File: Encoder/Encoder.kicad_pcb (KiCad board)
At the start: 2 copper layers, 50 x 40 mm, 58 parts, among them J1 Conn_01x02_Male, J2 Conn_01x04_Male, J3 Conn_01x04_Male, J4 Conn_01x04_Female, Q1 SSM3J332R, Q12 S8050, Q2 BSS138, Q3 SSM3J332R, SW1 SW_DIP_x05, SW2 SW_SPDT_White, SW3 SW_SPST, U1 AZ1084CD-3.3, U2 MAX3485, U3 AS5600, U4 STM32C011F4P6, Y1 48MHz

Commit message: 回路図pdf出力
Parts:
- C1: value 4.7uF -> 1uF; footprint Capacitor_SMD:C_0603_1608Metric -> Capacitor_SMD:C_0402_1005Metric
- D2, D3: footprint Diode_SMD:D_SMA_Handsoldering -> Diode_SMD:D_SMA
- JP1: footprint Connector_PinHeader_2.54mm:PinHeader_1x02_P2.54mm_Vertical -> Jumper:SolderJumper-2_P1.3mm_Open_TrianglePad1.0x1.5mm
- Q1, Q3, U1, U2, U4: moved to B.Cu
- Y1: footprint Crystal:Crystal_SMD_HC49-SD_HandSoldering -> Crystal:Crystal_SMD_HC49-SD; moved to B.Cu
- moved U2 86.3 mm to (-8.25, -45.8), turned to 180 degrees
- moved D5 84.7 mm to (-4.25, -56.5)
- moved D8 80.6 mm to (0.00, -56.5)
- moved D1 65.9 mm to (4.25, -56.5)
- moved U4 65.6 mm to (0.00, -38.2), turned to 90 degrees
- moved SW2 60.7 mm to (9.50, -41.8)
- moved SW3 55.9 mm to (-9.75, -42.0), turned to 90 degrees
- moved Y1 53.2 mm to (-8.50, -34.5), turned to -90 degrees
- moved U1 46.2 mm to (14.5, -69.8)
- moved Q3 41.3 mm to (32.0, -56.0), turned to 180 degrees
- moved Q1 39.7 mm to (36.2, -56.0), turned to 90 degrees
- moved J2 13.8 mm to (-10.2, -52.4)
- moved J1 12.8 mm to (7.50, -52.4)
- moved SW1 1.94 mm to (0.00, -43.0)
- moved U3 0.10 mm to (0.00, -30.0)

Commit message: 定期更新
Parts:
- C1, C12, C15, C2, C3, C4, C5, C6, C7, D2, D3, JP1, Q12, Q2, R1, R10, R12, R14, R2, R24, R27, R28, R29, R3, R30, R31, R32, R4, R5, R6, R7, R8, R9: moved to B.Cu
- moved R31 101.5 mm to (-8.91, -48.5)
- moved C5 99.5 mm to (-11.5, -28.5), turned to -90 degrees
- moved R29 98.8 mm to (-6.90, -41.1)
- moved C2 95.5 mm to (-4.38, -28.7), turned to 90 degrees
- moved C15 89.1 mm to (-8.92, -47.4)
- moved R24 88.0 mm to (0.00, -56.6), turned to 180 degrees
- moved C6 79.2 mm to (-11.5, -35.5), turned to 90 degrees
- moved JP1 75.8 mm to (-11.8, -48.6)
- moved Q2 75.1 mm to (9.65, -47.6)
- moved R2 74.2 mm to (18.6, -46.4), turned to 90 degrees
- moved C4 74.2 mm to (10.1, -33.7), turned to 180 degrees
- moved C12 72.8 mm to (-4.73, -37.3), turned to 180 degrees
- moved R28 72.7 mm to (-6.89, -46.1), turned to 180 degrees
- moved R10 69.3 mm to (11.1, -41.7), turned to -90 degrees
- moved C7 69.1 mm to (-4.63, -38.7), turned to 180 degrees
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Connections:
- U4 pad 2: unconnected-(U4-Pad2) -> OSC_IN
- U4 pad 3: unconnected-(U4-Pad3) -> OSC_OUT
- U4 pad 6: unconnected-(U4-Pad6) -> NRST
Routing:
- net OSC_IN: track 0.00 -> 0.69 mm

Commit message: 進捗
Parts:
- added H1: MountingHole_Pad, TestPoint:TestPoint_Pad_1.5x1.5mm, F.Cu at (49.1, -46.6)
- added H2: MountingHole_Pad, TestPoint:TestPoint_Pad_1.5x1.5mm, F.Cu at (45.5, -46.6)
- C8, C9: footprint Capacitor_SMD:C_0805_2012Metric_Pad1.18x1.45mm_HandSolder -> Capacitor_SMD:C_0805_2012Metric; moved to B.Cu
- D2, D3: value SBR1A40SA -> 1N5819WS; footprint Diode_SMD:D_SMA -> Diode_SMD:D_SOD-323_HandSoldering
- R11, R13: moved to B.Cu
- moved R11 56.8 mm to (19.6, -31.1), turned to -90 degrees
- moved C9 46.2 mm to (5.29, -24.3), turned to -90 degrees
- moved R1 36.4 mm to (-2.90, -48.1)
- moved R3 36.4 mm to (-2.90, -47.0)
- moved R6 36.4 mm to (-2.90, -44.7)
- moved R8 36.4 mm to (-2.90, -43.6)
- moved R5 36.4 mm to (-2.90, -45.8)
- moved R13 27.6 mm to (11.2, -35.6), turned to -90 degrees
- moved C8 25.0 mm to (17.7, -31.3), turned to -90 degrees
- moved Q2 11.5 mm to (21.1, -47.6), turned to -90 degrees
- moved R10 10.5 mm to (18.6, -49.1), turned to 90 degrees
- moved C4 8.96 mm to (7.08, -25.3), turned to -90 degrees
- moved C5 6.52 mm to (-12.3, -22.0), turned to 180 degrees
- moved Y1 5.69 mm to (-13.1, -29.8)
- moved C6 3.43 mm to (-14.0, -37.9), turned to 0 degrees
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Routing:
- net RS485_A: track 0.00 -> 25.5 mm
- net RS485_B: track 0.00 -> 19.8 mm
- net 主電源スイッチ: track 0.00 -> 9.49 mm
- net MainTX_RS485RX: track 0.00 -> 8.43 mm
- net Net-(Q12-Pad3): track 0.00 -> 8.43 mm
- net Net-(JP1-Pad2): track 0.00 -> 2.15 mm
- net Net-(Q12-Pad1): track 0.00 -> 1.77 mm
- net unconnected-(U4-Pad1): track 0.00 -> 0.69 mm
- net OSC_IN: track 0.69 -> 0.00 mm
- added copper zone on B.Cu, net /5VBAT
- added copper zone on B.Cu, net /S-S

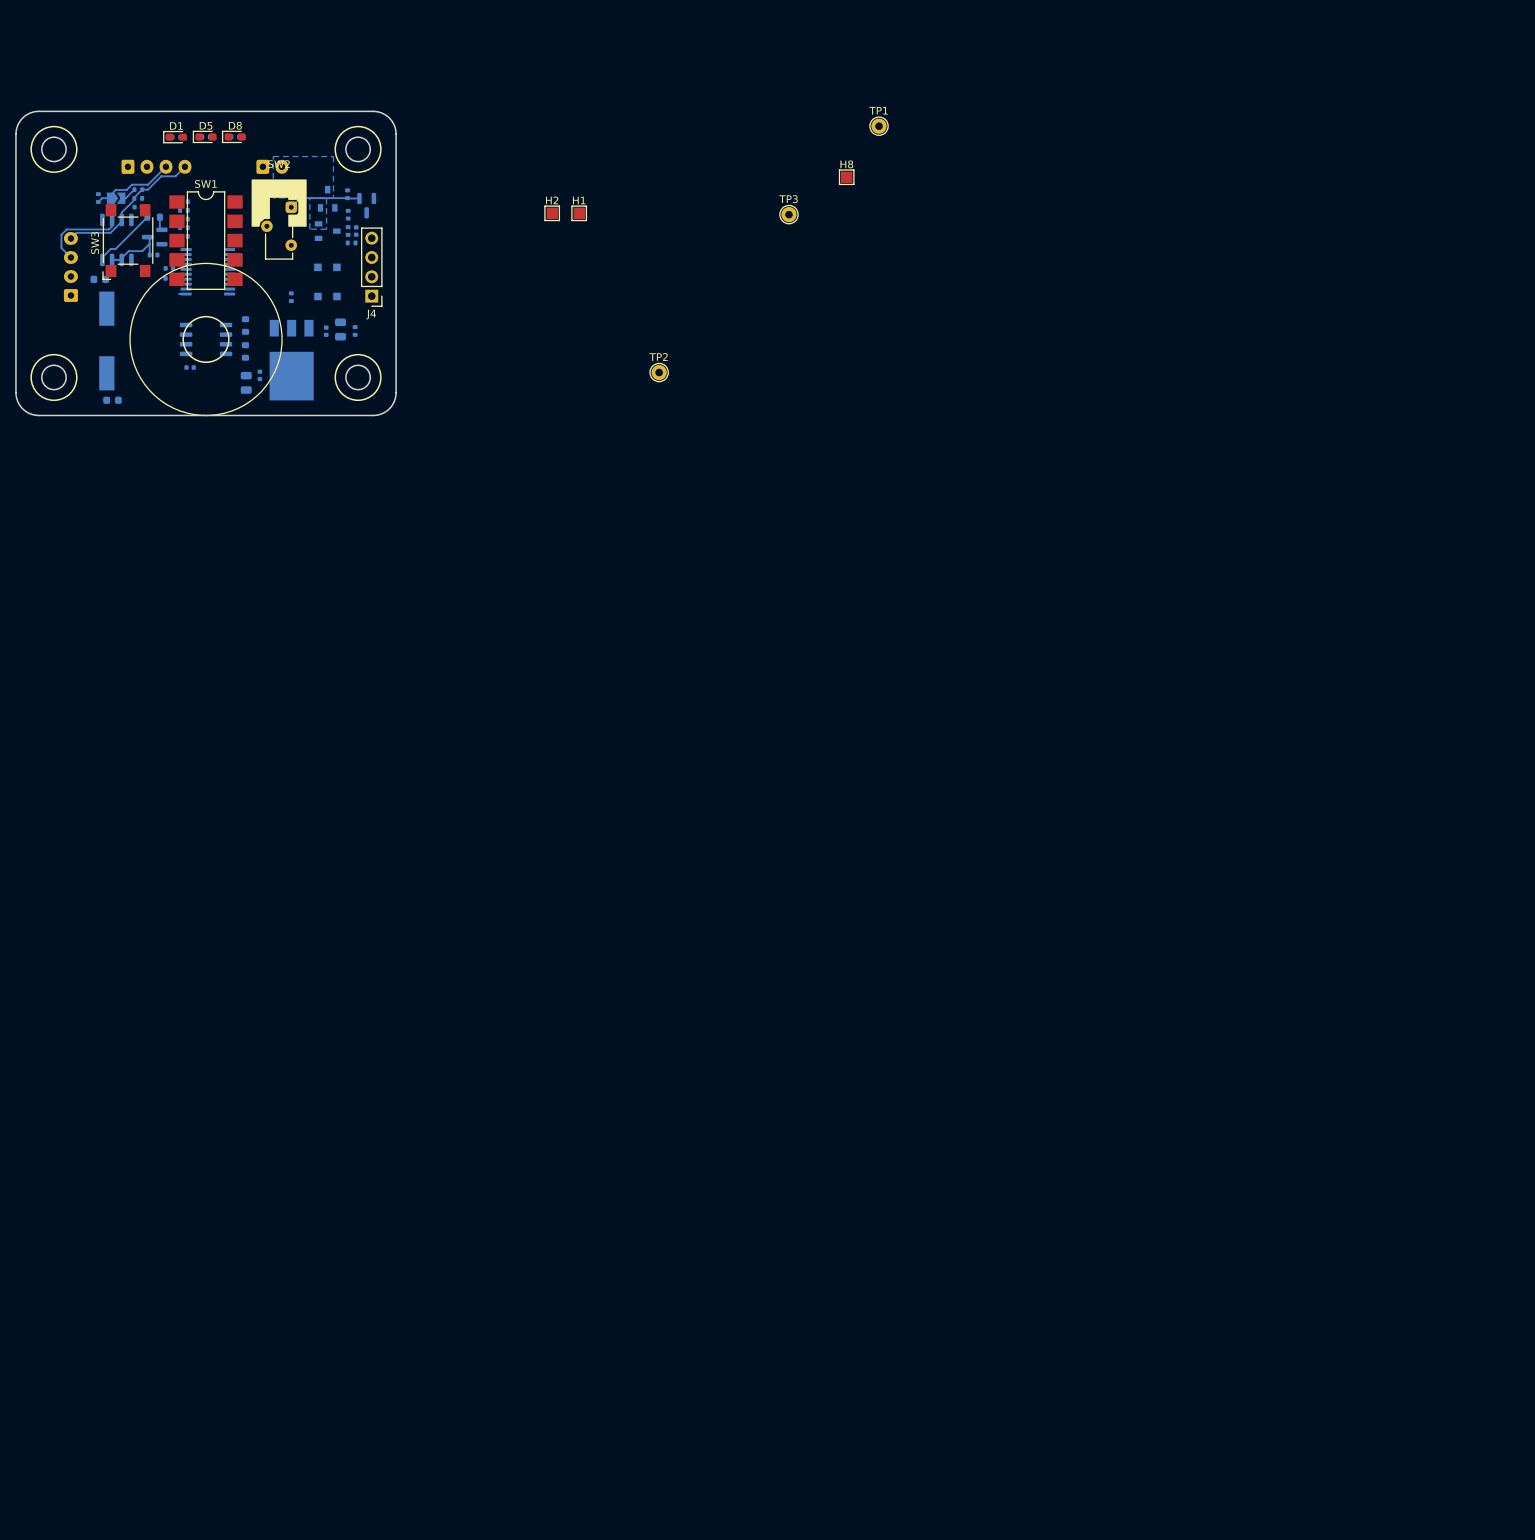
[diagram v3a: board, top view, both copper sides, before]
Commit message: エンコーダー基板配線完了
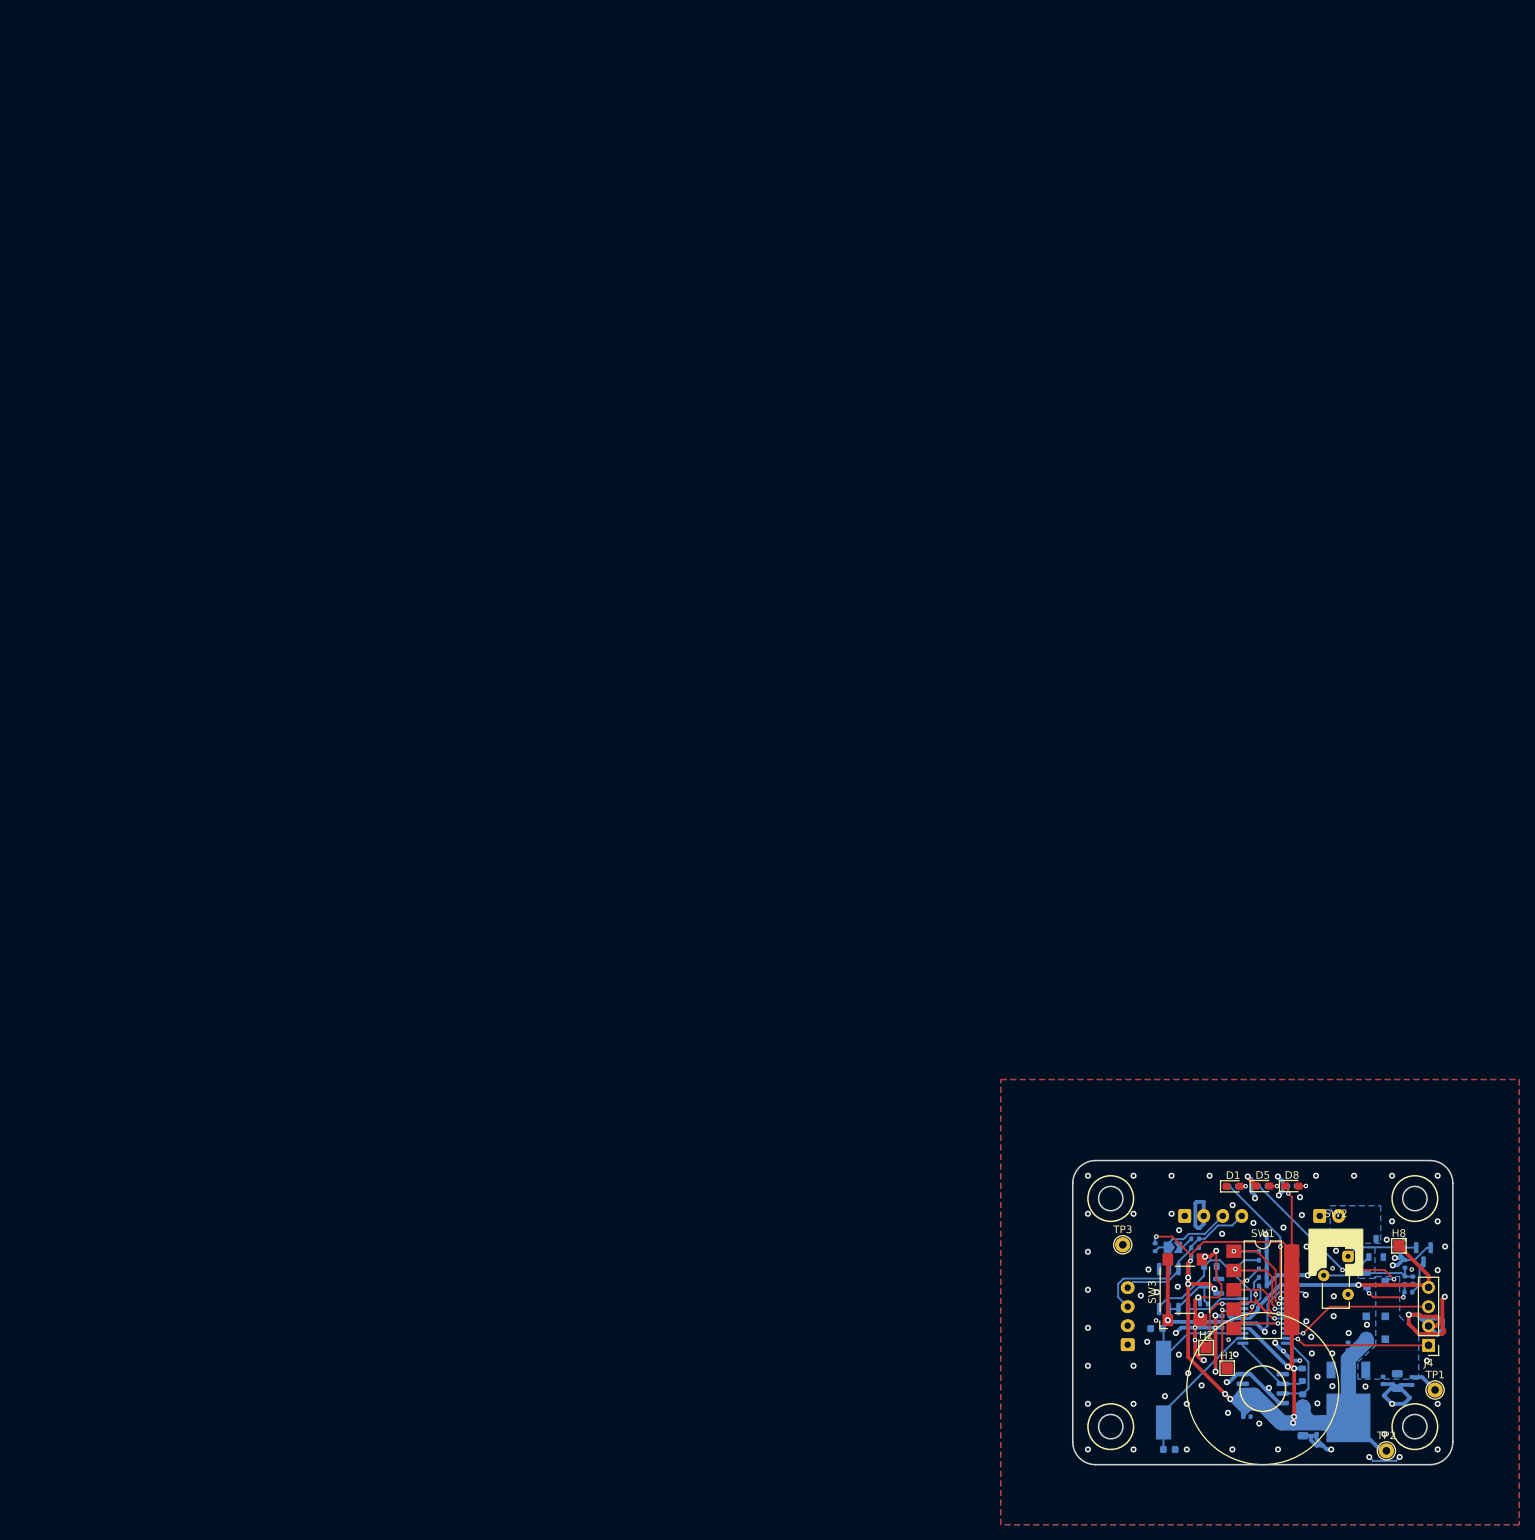
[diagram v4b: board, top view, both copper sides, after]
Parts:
- H1: value MountingHole_Pad -> UART1_TX
- H2: value MountingHole_Pad -> UART1_RX
- U4: value STM32C011F4P6 -> STM32C011F6P6
- moved R1 198.0 mm to (139.0, 90.0)
- moved R3 198.0 mm to (139.0, 91.1)
- moved R5 198.0 mm to (139.0, 92.2)
- moved R6 198.0 mm to (139.0, 93.4)
- moved R8 198.0 mm to (139.0, 94.5)
- moved C4 196.4 mm to (146.1, 113.5)
- moved C8 196.1 mm to (156.7, 107.0)
- moved R11 196.0 mm to (158.6, 107.0)
- moved R12 195.9 mm to (144.2, 109.6)
- moved C1 195.9 mm to (158.8, 93.7)
- moved C12 195.9 mm to (134.2, 100.0)
- moved C15 195.9 mm to (130.1, 90.6)
- moved C2 195.9 mm to (136.9, 111.7)
- moved C3 195.9 mm to (154.8, 106.9)
- moved C5 195.9 mm to (126.7, 116.0)
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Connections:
- H1 pad 1: unconnected-(H1-Pad1) -> Net-(H1-Pad1)
- H2 pad 1: unconnected-(H2-Pad1) -> Net-(H2-Pad1)
- R12 pad 2: I2C_SCL -> I2C1_SCL
- R14 pad 2: I2C_SDA -> I2C1_SDA
- R28 pad 2: MainTX_RS485RX -> MainTX2_RS485RX
- U2 pad 1: MainRX_RS485TX -> MainRX2_RS485TX
- U2 pad 4: MainTX_RS485RX -> MainTX2_RS485RX
- U3 pad 6: I2C_SDA -> I2C1_SDA
- U3 pad 7: I2C_SCL -> I2C1_SCL
- U4 pad 1: unconnected-(U4-Pad1) -> I2C1_SDA
- U4 pad 10: unconnected-(U4-Pad10) -> MainRX2_RS485TX
- U4 pad 11: unconnected-(U4-Pad11) -> MonitorLED0
- U4 pad 12: unconnected-(U4-Pad12) -> DIP_SW0
- U4 pad 13: unconnected-(U4-Pad13) -> DIP_SW1
- U4 pad 14: unconnected-(U4-Pad14) -> DIP_SW2
- U4 pad 15: unconnected-(U4-Pad15) -> DIP_SW3
- U4 pad 16: unconnected-(U4-Pad16) -> DIP_SW4
- U4 pad 18: unconnected-(U4-Pad18) -> TMS
- U4 pad 19: unconnected-(U4-Pad19) -> TCK
- U4 pad 20: unconnected-(U4-Pad20) -> I2C1_SCL
- U4 pad 7: unconnected-(U4-Pad7) -> Net-(H1-Pad1)
- U4 pad 8: unconnected-(U4-Pad8) -> Net-(H2-Pad1)
- U4 pad 9: unconnected-(U4-Pad9) -> MainTX2_RS485RX
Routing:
- net +3.3V: track 0.23 -> 168.6 mm, vias 0 -> 12
- net GND: track 0.00 -> 153.9 mm, vias 0 -> 103
- net NRST: track 0.00 -> 52.7 mm, vias 0 -> 2
- net VDD: track 0.00 -> 27.8 mm, vias 0 -> 2
- net TMS: track 0.00 -> 20.2 mm, vias 0 -> 1
- net MainTX2_RS485RX: track 0.00 -> 19.8 mm
- net OSC_IN: track 0.00 -> 19.4 mm
- net TCK: track 0.00 -> 19.1 mm, vias 0 -> 1
- net MonitorLED0: track 0.00 -> 18.3 mm, vias 0 -> 2
- net OSC_OUT: track 0.00 -> 15.7 mm
- net DIP_SW0: track 0.00 -> 15.5 mm, vias 0 -> 2
- net DIP_SW1: track 0.00 -> 14.9 mm, vias 0 -> 2
- net DIP_SW3: track 0.00 -> 14.4 mm, vias 0 -> 2
- net /S-S: track 0.00 -> 14.3 mm
- net DIP_SW4: track 0.00 -> 14.3 mm, vias 0 -> 2
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- added copper zone on B.Cu, net GND
- added copper zone on F.Cu, net GND
- added copper zone on B.Cu, net VDD

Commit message: LargeMD
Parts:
- moved R4 6.36 mm to (141.3, 80.0)
- moved R24 2.35 mm to (141.3, 81.2)
- moved R27 1.77 mm to (141.4, 82.3)
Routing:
- net GND: track 153.9 -> 271.7 mm, vias 103 -> 108
- net Net-(D1-Pad2): track 1.92 -> 6.97 mm
- net DIP_SW3: track 14.4 -> 11.8 mm
- net Net-(D5-Pad2): track 2.34 -> 4.56 mm

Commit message: LargeMDほぼ完成
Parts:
- moved H1 2.22 mm to (134.0, 103.1)
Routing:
- net Net-(H1-Pad1): track 10.8 -> 8.53 mm
- net GND: vias 108 -> 109
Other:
- board text added: "Designed by @cat_nekonekone"
- board text added: "Tomoshibi"
- board text added: "燈"
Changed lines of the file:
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@@
   )
   (footprint "TestPoint:TestPoint_Pad_1.5x1.5mm" (layer "F.Cu")
-    (at 134.31 105.31)
+    (at 134.04 103.11)
     (descr "SMD rectangular pad as test Point, square 1.5mm side length")
     (tags "test point SMD pad rectangle square")
@@
     )
   )
-  (gr_circle (center 139 108) (end 142 108) (layer "F.SilkS") (width 0.2) (fill none))
   (gr_circle (center 119 83) (end 122 83) (layer "F.SilkS") (width 0.2) (fill none))
   (gr_circle (center 159 83) (end 162 83) (layer "F.SilkS") (width 0.2) (fill none))
@@
   (gr_line (start 117 118) (end 161 118) (layer "Edge.Cuts") (width 0.2))
   (gr_arc (start 117 118) (mid 114.87868 117.12132) (end 114 115) (layer "Edge.Cuts") (width 0.2))
+  (gr_text "Designed by\n@cat_nekonekone" (at 139.24 115.01) (layer "F.SilkS")
+    (effects (font (size 0.9 0.9) (thickness 0.13)))
+  )
+  (gr_text "燈" (at 138.78 107.05) (layer "F.SilkS")
+    (effects (font (size 6 6) (thickness 0.42)))
+  )
+  (gr_text "Tomoshibi" (at 138.85 112.15) (layer "F.SilkS")
+    (effects (font (size 1.8 1.8) (thickness 0.21)))
+  )
   (segment (start 158.75 93.26) (end 157.72 93.26) (width 0.25) (layer "B.Cu") (net 1))
   (segment (start 157.26 92.8) (end 152.7 92.8) (width 0.25) (layer "B.Cu") (net 1))
@@
   (via (at 116 85) (size 0.8) (drill 0.4) (layers "F.Cu" "B.Cu") (free) (net 3))
   (via (at 150.3 100.69) (size 0.8) (drill 0.4) (layers "F.Cu" "B.Cu") (free) (net 3))
-  (via (at 135.44 103.49) (size 0.8) (drill 0.4) (layers "F.Cu" "B.Cu") (free) (net 3))
+  (via (at 135.56 103.41) (size 0.8) (drill 0.4) (layers "F.Cu" "B.Cu") (free) (net 3))
   (via (at 127.57 100.68) (size 0.8) (drill 0.4) (layers "F.Cu" "B.Cu") (free) (net 3))
   (via (at 116 100) (size 0.8) (drill 0.4) (layers "F.Cu" "B.Cu") (free) (net 3))
@@
   (via (at 130.09 101.6) (size 0.6) (drill 0.3) (layers "F.Cu" "B.Cu") (free) (net 3))
   (via (at 139.81 107.9) (size 0.8) (drill 0.4) (layers "F.Cu" "B.Cu") (free) (net 3))
+  (via (at 133.79 104.78) (size 0.8) (drill 0.4) (layers "F.Cu" "B.Cu") (free) (net 3))
   (via (at 137.77 86.21) (size 0.8) (drill 0.4) (layers "F.Cu" "B.Cu") (free) (net 3))
   (segment (start 128.27 99.98) (end 133.68 99.98) (width 0.5) (layer "B.Cu") (net 3))
@@
   (segment (start 140.995 99.425) (end 140.99 99.43) (width 0.25) (layer "B.Cu") (net 26))
   (segment (start 142.1025 99.425) (end 140.995 99.425) (width 0.25) (layer "B.Cu") (net 26))
-  (segment (start 133.669487 104.669487) (end 134.31 105.31) (width 0.25) (layer "F.Cu") (net 27))
-  (segment (start 133.669487 97.639502) (end 133.669487 104.669487) (width 0.25) (layer "F.Cu") (net 27))
+  (segment (start 133.669487 97.639502) (end 133.669487 102.590513) (width 0.25) (layer "F.Cu") (net 27))
+  (segment (start 133.669487 102.739487) (end 133.669487 102.590513) (width 0.25) (layer "F.Cu") (net 27))
+  (segment (start 134.04 103.11) (end 133.669487 102.739487) (width 0.25) (layer "F.Cu") (net 27))
   (via (at 133.669487 97.639502) (size 0.6) (drill 0.3) (layers "F.Cu" "B.Cu") (net 27))
   (segment (start 133.854985 97.825) (end 134.992609 97.825) (width 0.25) (layer "B.Cu") (net 27))

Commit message: 製造ファイル出力
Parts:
- moved H2 2.29 mm to (133.6, 103.6)
- moved H1 2.21 mm to (136.2, 103.6)
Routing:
- net GND: track 271.7 -> 266.0 mm, vias 109 -> 110
- net Net-(H2-Pad1): track 9.98 -> 11.4 mm
- net Net-(H1-Pad1): track 8.53 -> 9.92 mm
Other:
- board text added: "+3.3V"
- board text added: "GND"
- board text added: "JLCJLCJLCJLC"
- board text added: "NRST"
- board text added: "PA11"
- board text added: "PA4"
- board text added: "PA5"
- board text added: "PA6"
- board text added: "PA7"
- board text added: "PA8"
- board text added: "POWER"
- board text added: "RST"
- board text added: "RX"
- board text added: "RX1:PA1"
- board text added: "RX2:PA3"
- board text added: "SCL1:PB6"
- board text added: "SDA1:PB7"
- board text added: "SWCLK"
- board text added: "SWDIO"
- board text added: "TX"
- board text added: "TX1:PA0"
- board text added: "TX2:PA2"
- board text added: "VDD"
- board text added: "[Enc]"
- board text added: "[Pad]"
- board text added: "[RS485]"
